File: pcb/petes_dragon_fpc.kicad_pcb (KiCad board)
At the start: 2 copper layers, 154.6 x 140.5 mm, 201 parts, among them J1 JST-PH-3P

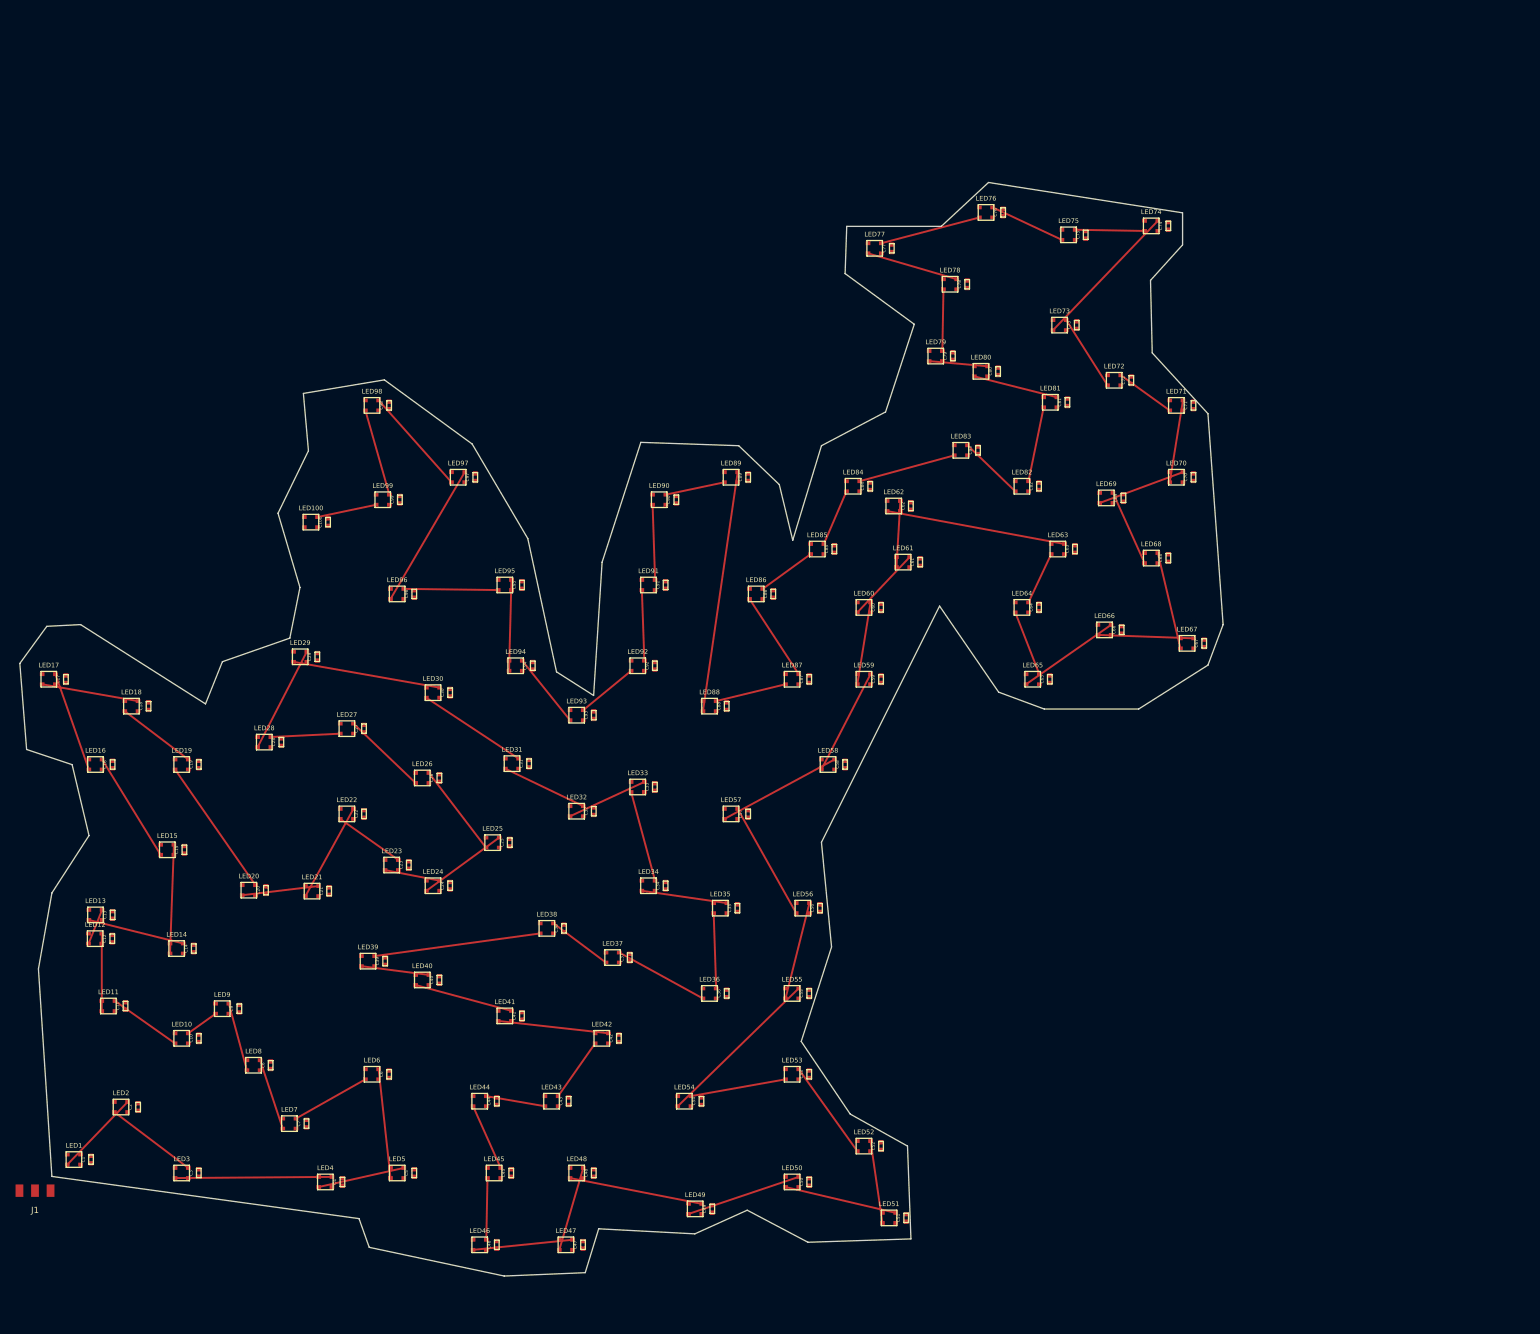
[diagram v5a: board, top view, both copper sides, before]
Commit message: feat(pcb): route full 3-rail power architecture with 5V bus, GND vias, and ground plane
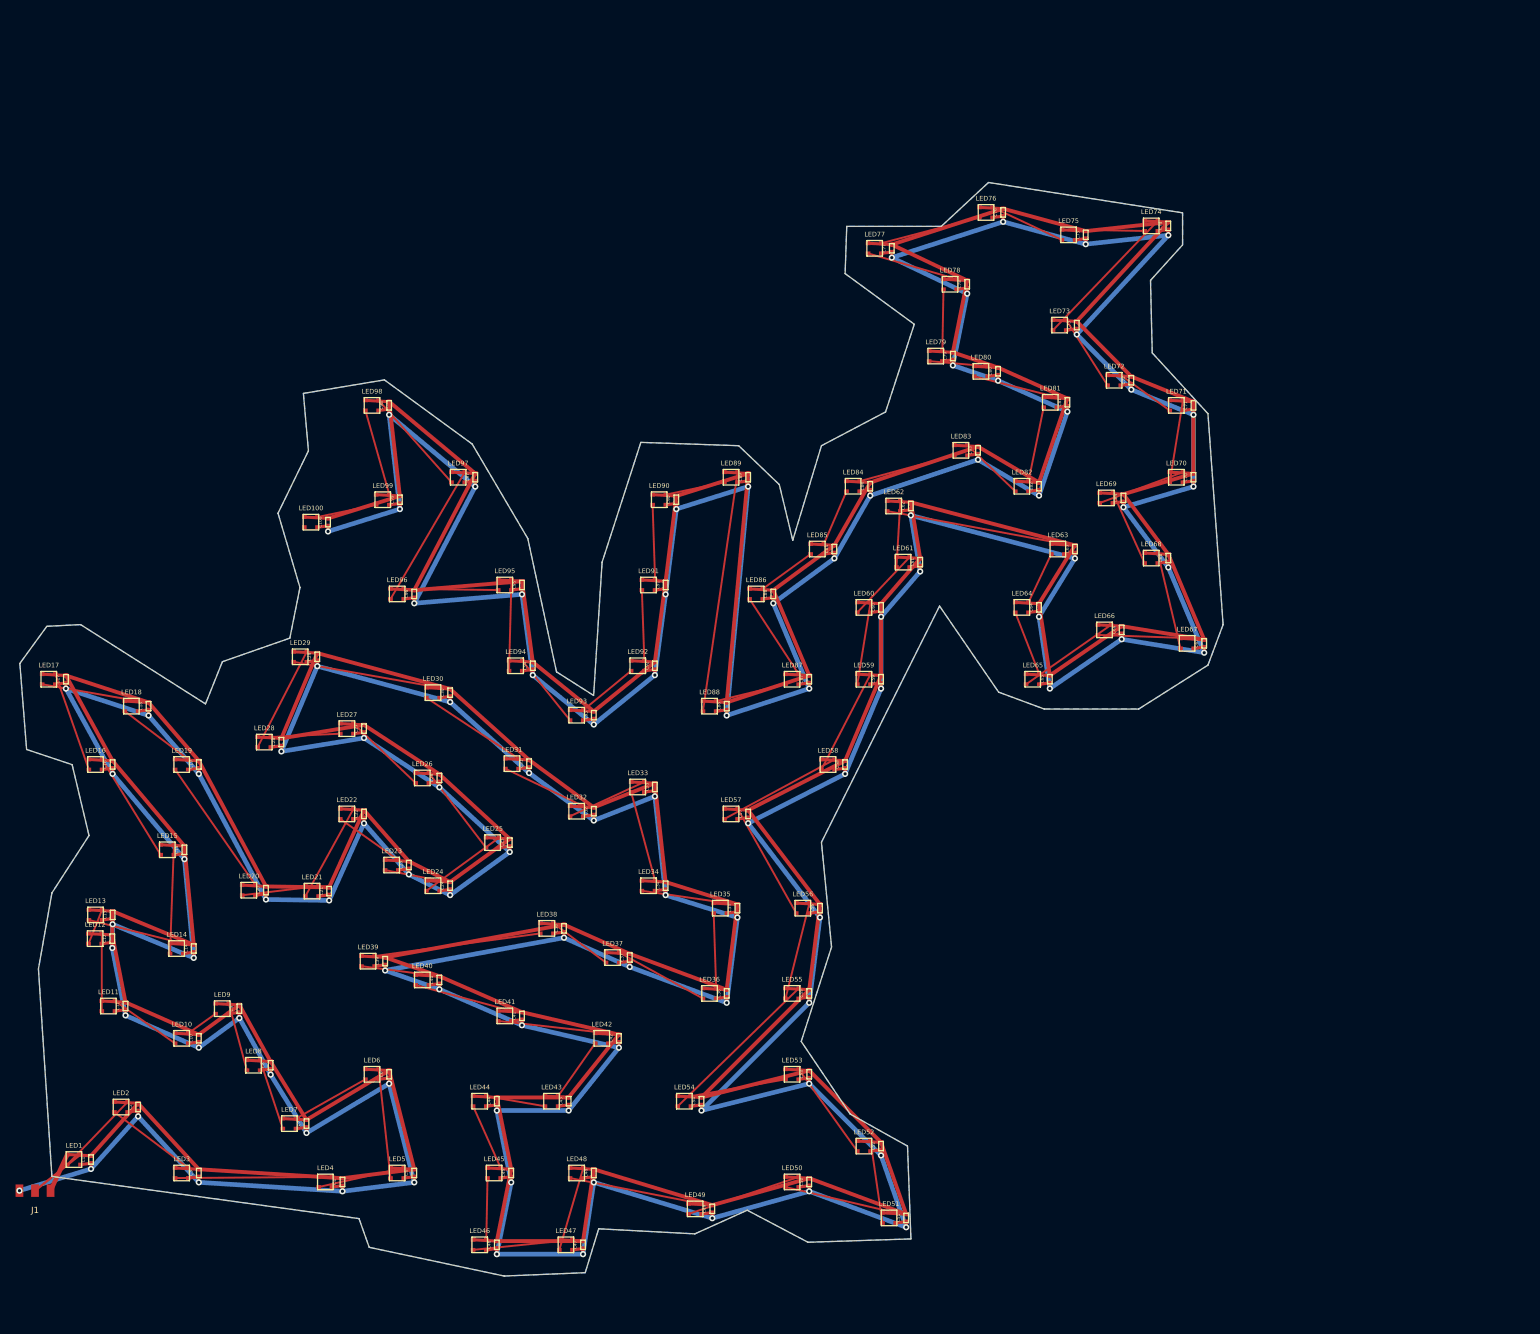
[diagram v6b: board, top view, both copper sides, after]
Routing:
- net +5V: track 0.00 -> 1451.7 mm
- net GND: track 0.00 -> 1358.8 mm, vias 0 -> 101
- net DATA_1: track 0.00 -> 7.47 mm
- added copper zone on B.Cu, net GND
